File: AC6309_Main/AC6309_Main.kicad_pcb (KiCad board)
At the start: 2 copper layers, 8 parts, among them J1 Address Bus, J2 Data and Control, U1 HD63B09P, U2 W24257, U3 28C256, U4 74HCT00, U5 TMP68681, U6 MAX3232

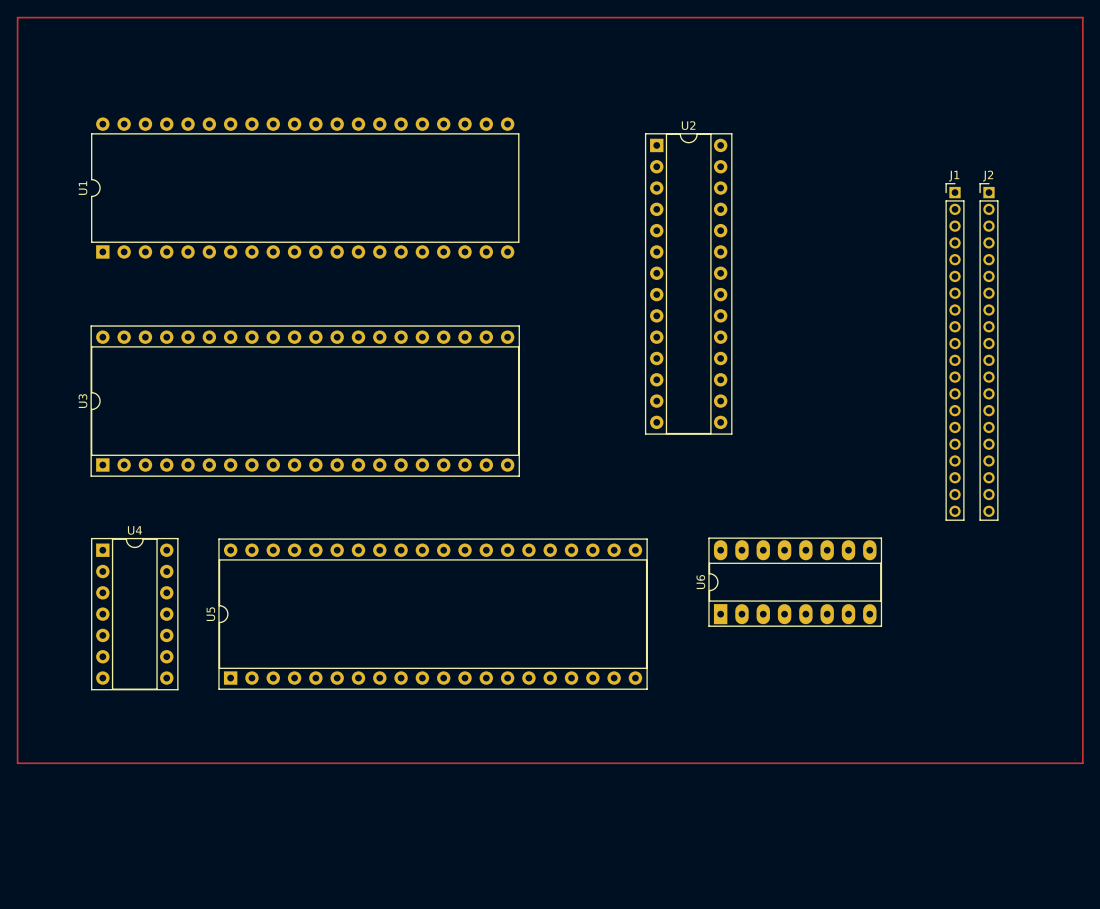
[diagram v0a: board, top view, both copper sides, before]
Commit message: Adding 74HC138 to the address decoder
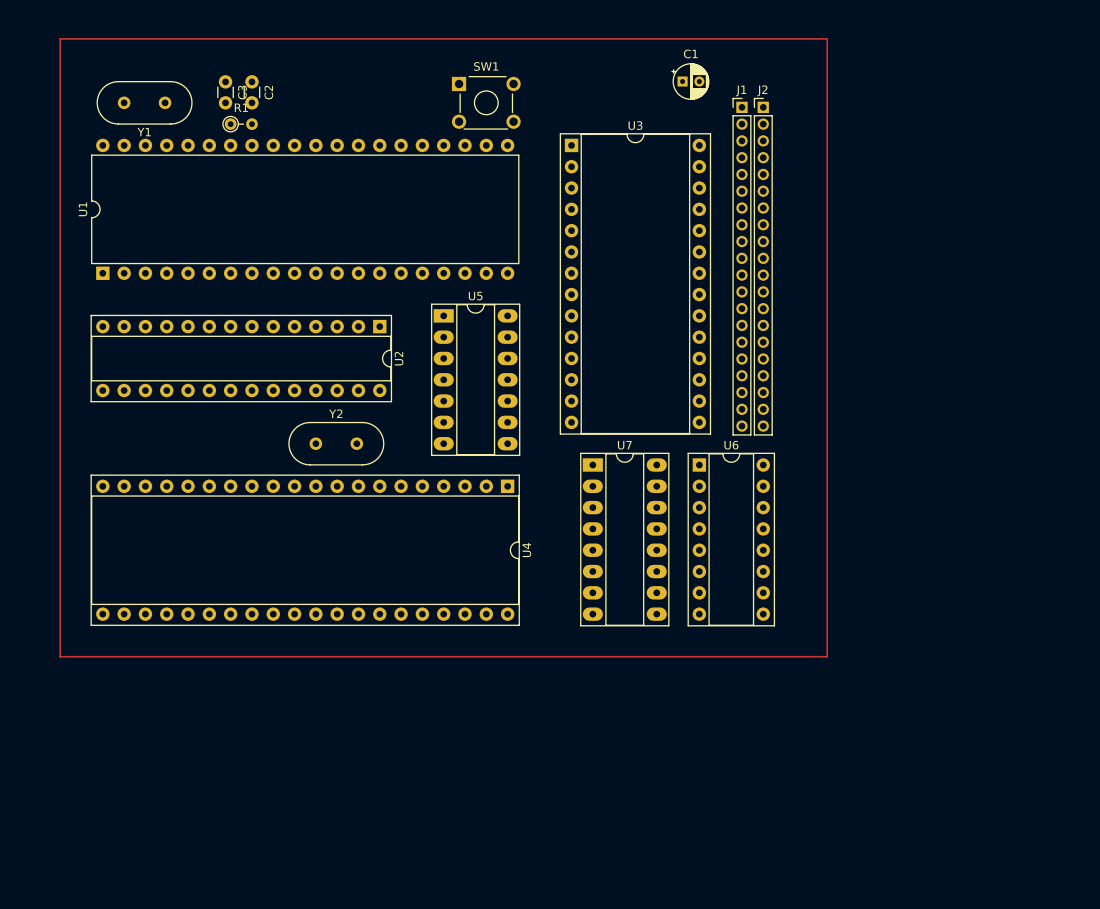
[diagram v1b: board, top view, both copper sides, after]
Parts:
- added C1: 100 uF, Capacitor_THT:CP_Radial_D4.0mm_P2.00mm, F.Cu at (119.9, 30.5)
- added C2: 15pF, Capacitor_THT:C_Disc_D3.0mm_W1.6mm_P2.50mm, F.Cu at (68.6, 30.5)
- added C3: 15pF, Capacitor_THT:C_Disc_D3.0mm_W1.6mm_P2.50mm, F.Cu at (65.4, 30.5)
- added R1: 2K2, Resistor_THT:R_Axial_DIN0204_L3.6mm_D1.6mm_P2.54mm_Vertical, F.Cu at (66.0, 35.6)
- added SW1: Reset, Button_Switch_THT:SW_TH_Tactile_Omron_B3F-10xx, F.Cu at (93.3, 30.8)
- added U6: 74HC138, Package_DIP:DIP-16_W7.62mm_Socket, F.Cu at (121.9, 76.2)
- added Y1: 7.3728 MHz, Crystal:Crystal_HC49-U_Vertical, F.Cu at (58.2, 33.0)
- added Y2: 1.8432 MHz, Crystal:Crystal_HC49-U_Vertical, F.Cu at (76.2, 73.7)
- J1: value Address Bus -> Address
- U3: footprint Package_DIP:DIP-40_W15.24mm_Socket -> Package_DIP:DIP-28_W15.24mm_Socket
- U5: renamed from U4; footprint Package_DIP:DIP-14_W7.62mm_Socket -> Package_DIP:DIP-14_W7.62mm_Socket_LongPads
- moved U3 67.6 mm to (106.7, 38.1), turned to 0 degrees
- moved U5 49.3 mm to (91.4, 58.4)
- moved U4 40.2 mm to (99.1, 78.7), turned to -90 degrees
- moved U2 39.5 mm to (83.8, 59.7), turned to -90 degrees
- moved J2 28.8 mm to (129.5, 33.6)
- moved J1 27.4 mm to (127.0, 33.6)
- moved U7 23.4 mm to (109.2, 76.2), turned to 0 degrees
- moved U1 2.54 mm to (50.8, 53.3)
- renumbered U5 to U4, U6 to U7
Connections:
- net Net-(U2-~{OE}) renamed //READ
- net Net-(U2-~{WE}) renamed //WRITE
- net Net-(U3-~{CS}) renamed //ROM_CS
- J2 pad 10: GND -> /8000_CS
- J2 pad 11: unconnected-(J2-Pin_11-Pad11) -> /9000_CS
- J2 pad 12: unconnected-(J2-Pin_12-Pad12) -> /A000_CS
- J2 pad 13: unconnected-(J2-Pin_13-Pad13) -> /B000_CS
- J2 pad 14: unconnected-(J2-Pin_14-Pad14) -> /R/W
- J2 pad 15: VCC -> unconnected-(J2-Pin_15-Pad15)
- U1 pad 32: Net-(U1-R/~{W}) -> /R/W
- U1 pad 34: Net-(U1-E) -> /E
- U1 pad 35: unconnected-(U1-Q-Pad35) -> /Q
- U1 pad 5: unconnected-(U1-BS-Pad5) -> /BS
- U1 pad 6: unconnected-(U1-BA-Pad6) -> /BA
- U4 pad 32: unconnected-(U5-X1/CLK-Pad32) -> Net-(U4-X1/CLK)
- U4 pad 33: unconnected-(U5-X2-Pad33) -> Net-(U4-X2)
- U5 pad 10: Net-(U1-E) -> Net-(U5-Pad10)
- U5 pad 11: Net-(U4-Pad11) -> Net-(U5-Pad10)
- U5 pad 12: Net-(U1-R/~{W}) -> /R/W
- U5 pad 13: Net-(U1-R/~{W}) -> /R/W
- U5 pad 4: Net-(U1-R/~{W}) -> /R/W
- U5 pad 5: Net-(U1-E) -> /E
- U5 pad 9: Net-(U4-Pad11) -> /E

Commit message: Added resistor networks. Updated PCB layout. Added temporary freeroute traces.
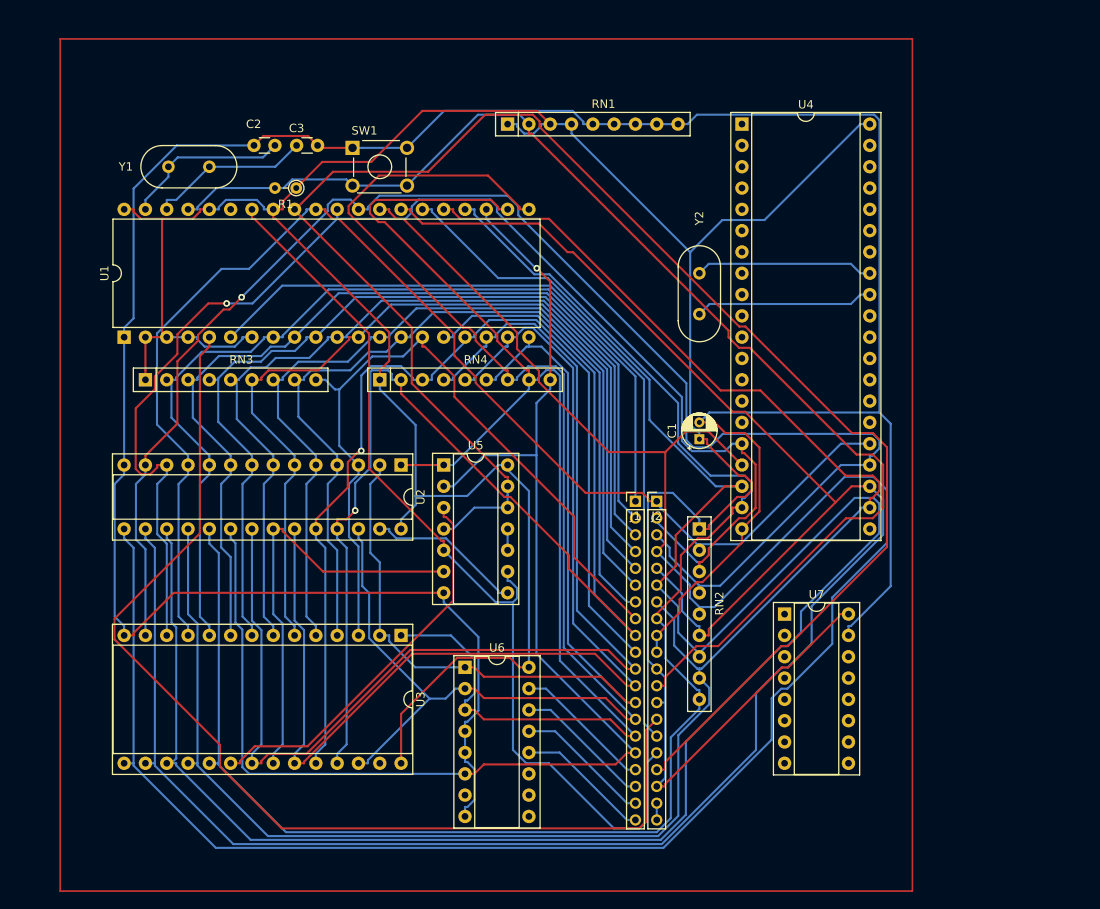
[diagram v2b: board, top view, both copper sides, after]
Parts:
- added RN1: R_Network08, Resistor_THT:R_Array_SIP9, F.Cu at (99.1, 35.6)
- added RN2: R_Network08, Resistor_THT:R_Array_SIP9, F.Cu at (121.9, 83.8)
- added RN3: R_Network08, Resistor_THT:R_Array_SIP9, F.Cu at (55.9, 66.0)
- added RN4: R_Network08, Resistor_THT:R_Array_SIP9, F.Cu at (83.8, 66.0)
- U5: footprint Package_DIP:DIP-14_W7.62mm_Socket_LongPads -> Package_DIP:DIP-14_W7.62mm_Socket
- U7: footprint Package_DIP:DIP-16_W7.62mm_Socket_LongPads -> Package_DIP:DIP-16_W7.62mm_Socket
- Y1, Y2: footprint Crystal:Crystal_HC49-U_Vertical -> Crystal:Crystal_HC49-4H_Vertical
- moved U3 61.9 mm to (86.4, 96.5), turned to -90 degrees
- moved U4 51.4 mm to (127.0, 35.6), turned to 0 degrees
- moved Y2 50.0 mm to (121.9, 53.3), turned to -90 degrees
- moved J1 48.6 mm to (114.3, 80.5)
- moved J2 48.6 mm to (116.8, 80.5)
- moved C1 42.7 mm to (121.9, 73.1), turned to 90 degrees
- moved U6 36.9 mm to (94.0, 100.3)
- moved U7 29.0 mm to (132.1, 94.0)
- moved U5 17.8 mm to (91.4, 76.2)
- moved U2 16.7 mm to (86.4, 76.2)
- moved SW1 14.8 mm to (80.6, 38.4)
- moved C3 11.4 mm to (73.9, 38.1), turned to 0 degrees
- moved R1 10.9 mm to (73.9, 43.2), turned to 180 degrees
- moved Y1 9.27 mm to (63.5, 40.6)
- moved C2 8.06 mm to (71.3, 38.1), turned to 180 degrees
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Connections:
- J1 pad 17: (no net) -> /8000_CS
- J1 pad 18: (no net) -> /9000_CS
- J1 pad 19: (no net) -> /A000_CS
- J1 pad 20: (no net) -> /B000_CS
- J2 pad 10: /8000_CS -> GND
- J2 pad 11: /9000_CS -> VCC
- J2 pad 12: /A000_CS -> //RESET
- J2 pad 13: /B000_CS -> VCC
- J2 pad 14: /R/W -> /BS
- J2 pad 15: unconnected-(J2-Pin_15-Pad15) -> /BA
- J2 pad 16: VCC -> /E
- J2 pad 17: (no net) -> /R/W
- J2 pad 18: (no net) -> VCC
- J2 pad 19: (no net) -> Net-(J2-Pin_19)
- J2 pad 20: (no net) -> Net-(J2-Pin_19)
- R1 pad 2: Net-(U1-~{RESET}) -> //RESET
- SW1 pad 2: Net-(U1-~{RESET}) -> //RESET
- U1 pad 37: Net-(U1-~{RESET}) -> //RESET
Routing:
- net VCC: track 0.00 -> 377.8 mm
- net GND: track 0.00 -> 345.5 mm
- net /D3: track 0.00 -> 262.4 mm
- net /D5: track 0.00 -> 254.8 mm
- net /D4: track 0.00 -> 253.6 mm
- net /D6: track 0.00 -> 219.1 mm
- net /R/W: track 0.00 -> 197.9 mm
- net /D7: track 0.00 -> 188.3 mm
- net /D2: track 0.00 -> 186.2 mm, vias 0 -> 1
- net /A13: track 0.00 -> 168.8 mm
- net /D1: track 0.00 -> 163.9 mm, vias 0 -> 1
- net /A15: track 0.00 -> 163.4 mm, vias 0 -> 1
- net /A14: track 0.00 -> 156.1 mm
- net /D0: track 0.00 -> 154.4 mm
- net /A8: track 0.00 -> 152.3 mm, vias 0 -> 1
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
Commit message: Replaced UART. Updates on Readme .
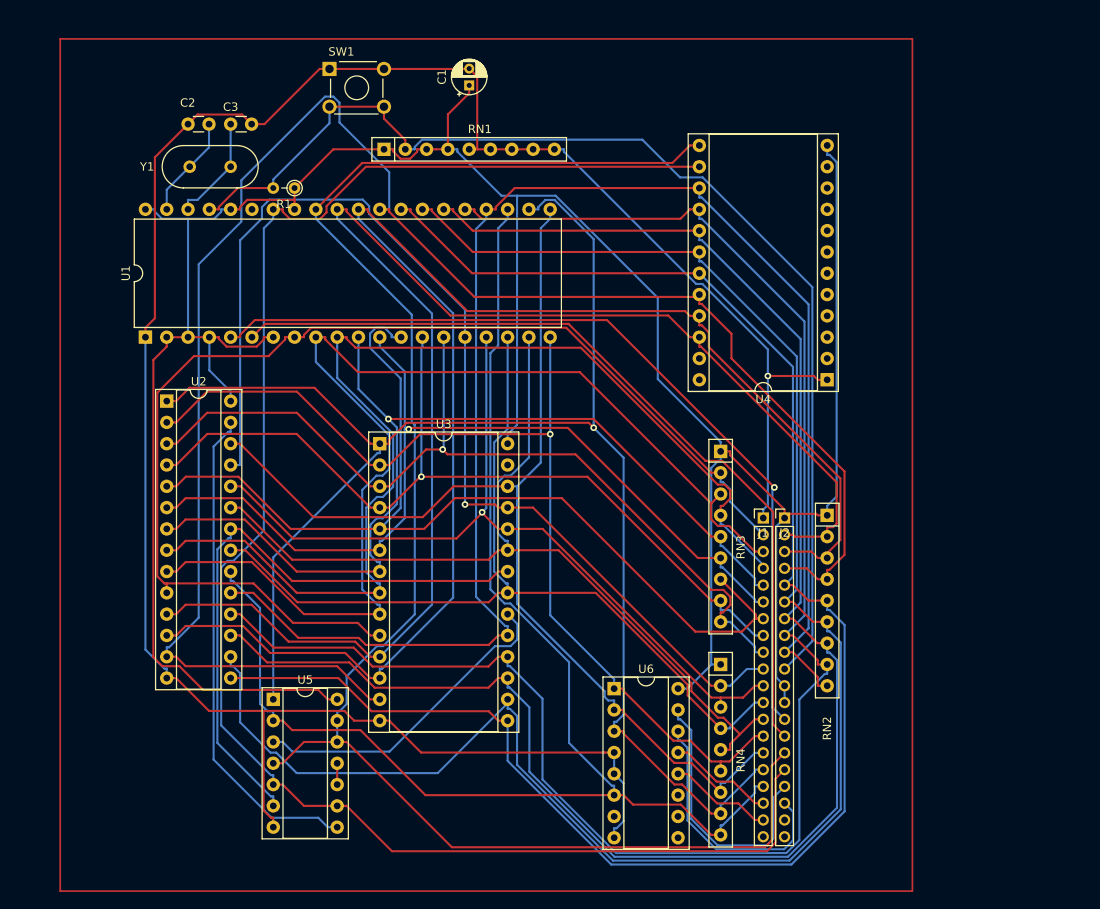
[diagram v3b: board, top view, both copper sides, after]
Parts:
- removed U7: MAX3232, Package_DIP:DIP-16_W7.62mm_Socket
- removed Y2: 1.8432 MHz, Crystal:Crystal_HC49-4H_Vertical
- U4: value TMP68681 -> MC68B50; footprint Package_DIP:DIP-40_W15.24mm_Socket -> Package_DIP:DIP-24_W15.24mm_Socket
- moved RN3 69.1 mm to (124.5, 74.6), turned to -90 degrees
- moved RN4 52.9 mm to (124.5, 100.0), turned to -90 degrees
- moved C1 50.3 mm to (94.5, 30.9)
- moved U5 34.5 mm to (71.1, 104.1)
- moved U4 32.1 mm to (137.2, 66.0), turned to 180 degrees
- moved U2 29.0 mm to (58.4, 68.6), turned to 0 degrees
- moved U3 23.0 mm to (83.8, 73.7), turned to 0 degrees
- moved U6 18.0 mm to (111.8, 102.9)
- moved J2 15.4 mm to (132.1, 82.5)
- moved J1 15.4 mm to (129.5, 82.5)
- moved RN2 15.3 mm to (137.2, 82.2)
- moved RN1 15.0 mm to (84.3, 38.6)
- moved SW1 9.80 mm to (77.8, 29.0)
- moved C3 8.26 mm to (66.0, 35.6)
- moved C2 8.26 mm to (63.5, 35.6)
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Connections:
- J1 pad 1: /A0 -> GND
- J1 pad 10: /A9 -> /A8
- J1 pad 11: /A10 -> /A9
- J1 pad 12: /A11 -> /A10
- J1 pad 13: /A12 -> /A11
- J1 pad 14: /A13 -> /A12
- J1 pad 15: /A14 -> /A13
- J1 pad 16: /A15 -> /A14
- J1 pad 17: /8000_CS -> /A15
- J1 pad 18: /9000_CS -> /A000_CS
- J1 pad 19: /A000_CS -> /B000_CS
- J1 pad 2: /A1 -> /A0
- J1 pad 20: /B000_CS -> unconnected-(J1-Pin_20-Pad20)
- J1 pad 3: /A2 -> /A1
- J1 pad 4: /A3 -> /A2
- J1 pad 5: /A4 -> /A3
- J1 pad 6: /A5 -> /A4
- J1 pad 7: /A6 -> /A5
- J1 pad 8: /A7 -> /A6
- J1 pad 9: /A8 -> /A7
- J2 pad 1: /D0 -> VCC
- J2 pad 10: GND -> //RESET
- J2 pad 12: //RESET -> VCC
- J2 pad 13: VCC -> /BS
- J2 pad 14: /BS -> /BA
- J2 pad 15: /BA -> /R/W
- J2 pad 17: /R/W -> /8000_CS
- J2 pad 18: VCC -> /9000_CS
- J2 pad 19: Net-(J2-Pin_19) -> unconnected-(J2-Pin_19-Pad19)
- J2 pad 2: /D1 -> /D0
- J2 pad 20: Net-(J2-Pin_19) -> unconnected-(J2-Pin_20-Pad20)
- J2 pad 3: /D2 -> /D1
- J2 pad 4: /D3 -> /D2
- J2 pad 5: /D4 -> /D3
- J2 pad 6: /D5 -> /D4
- J2 pad 7: /D6 -> /D5
- J2 pad 8: /D7 -> /D6
- J2 pad 9: GND -> /D7
- U4 pad 1: unconnected-(U4-A1-Pad1) -> GND
- U4 pad 12: unconnected-(U4-OP1-Pad12) -> VCC
- U4 pad 13: unconnected-(U4-OP3-Pad13) -> /R/W
- U4 pad 14: unconnected-(U4-OP5-Pad14) -> /E
- U4 pad 15: unconnected-(U4-OP7-Pad15) -> /D7
- U4 pad 16: /D1 -> /D6
- U4 pad 17: /D3 -> /D5
- U4 pad 18: /D5 -> /D4
- U4 pad 19: /D7 -> /D3
- U4 pad 20: GND -> /D2
- U4 pad 21: unconnected-(U4-INTRN-Pad21) -> /D1
- U4 pad 22: /D6 -> /D0
- U4 pad 23: /D4 -> unconnected-(U4-~{DCD}-Pad23)
- U4 pad 24: /D2 -> unconnected-(U4-~{CTS}-Pad24)
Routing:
- net /E: track 112.2 -> 201.5 mm
- net GND: track 345.5 -> 272.6 mm, vias 0 -> 1
- net /D3: track 262.4 -> 200.9 mm
- net /D5: track 254.8 -> 202.2 mm
- net /D4: track 253.6 -> 212.4 mm
- net //WRITE: track 18.7 -> 59.3 mm
- net /A13: track 168.8 -> 130.4 mm
- net /A10: track 142.0 -> 107.3 mm
- net /A14: track 156.1 -> 187.8 mm, vias 0 -> 1
- net /A11: track 136.0 -> 108.4 mm
- net /A0: track 113.2 -> 140.0 mm
- net /BS: track 128.0 -> 102.4 mm, vias 0 -> 1
- net /D2: track 186.2 -> 211.1 mm, vias 1 -> 0
- net VCC: track 377.8 -> 353.1 mm
- net /A1: track 111.7 -> 134.7 mm
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
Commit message: Schematics revision 1, Digital file, etc.
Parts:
- added J3: FTDI Header, Connector_PinHeader_2.54mm:PinHeader_1x06_P2.54mm_Vertical, F.Cu at (129.5, 116.8)
- J1, J2: footprint Connector_PinHeader_2.00mm:PinHeader_1x20_P2.00mm_Vertical -> Connector_PinHeader_2.54mm:PinHeader_1x20_P2.54mm_Vertical
- moved RN1 83.8 mm to (76.2, 121.9), turned to 180 degrees
- moved C1 83.0 mm to (121.9, 109.2)
- moved U5 70.8 mm to (53.3, 35.6)
- moved RN2 50.1 mm to (106.7, 121.9), turned to 180 degrees
- moved U4 44.2 mm to (102.9, 94.0), turned to 90 degrees
- moved J2 43.5 mm to (105.3, 116.8), turned to -90 degrees
- moved RN4 41.7 mm to (83.8, 109.2), turned to 180 degrees
- moved J1 39.9 mm to (105.3, 114.3), turned to -90 degrees
- moved RN3 36.1 mm to (114.3, 109.2), turned to 180 degrees
- moved C2 35.6 mm to (99.1, 35.7), turned to 90 degrees
- moved C3 33.1 mm to (99.1, 38.3), turned to -90 degrees
- moved SW1 30.7 mm to (107.8, 35.6)
- moved U2 30.6 mm to (61.0, 99.1), turned to 180 degrees
- moved U1 29.6 mm to (71.1, 35.6), turned to 0 degrees
- moved U6 26.2 mm to (87.6, 92.7), turned to -90 degrees
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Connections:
- J2 pad 11: VCC -> //NMI
- J2 pad 12: VCC -> //IRQ
- J2 pad 13: /BS -> //FIRQ
- J2 pad 14: /BA -> //HALT
- RN1 pad 3: VCC -> //NMI
- RN1 pad 4: VCC -> //IRQ
- RN1 pad 5: GND -> //FIRQ
- RN1 pad 6: GND -> //DMABREQ
- RN1 pad 7: GND -> //HALT
- RN1 pad 8: GND -> /MRDY
- U1 pad 2: VCC -> //NMI
- U1 pad 3: VCC -> //IRQ
- U1 pad 33: VCC -> //DMABREQ
- U1 pad 36: VCC -> /MRDY
- U1 pad 4: VCC -> //FIRQ
- U1 pad 40: VCC -> //HALT
- U1 pad 5: /BS -> unconnected-(U1-BS-Pad5)
- U1 pad 6: /BA -> unconnected-(U1-BA-Pad6)
- U4 pad 10: unconnected-(U4-CS1-Pad10) -> /A13
- U4 pad 11: unconnected-(U4-RS-Pad11) -> /A0
- U4 pad 2: unconnected-(U4-Rx_Data-Pad2) -> Net-(J3-Pin_3)
- U4 pad 23: unconnected-(U4-~{DCD}-Pad23) -> GND
- U4 pad 24: unconnected-(U4-~{CTS}-Pad24) -> Net-(U4-~{CTS})
- U4 pad 3: unconnected-(U4-Rx_CLK-Pad3) -> /E
- U4 pad 4: unconnected-(U4-Tx_CLK-Pad4) -> /E
- U4 pad 5: unconnected-(U4-~{RTS}-Pad5) -> Net-(U4-~{CTS})
- U4 pad 6: unconnected-(U4-Tx_Data-Pad6) -> Net-(J3-Pin_2)
- U4 pad 7: unconnected-(U4-~{IRQ}-Pad7) -> //IRQ
- U4 pad 8: unconnected-(U4-CS0-Pad8) -> /A15
- U4 pad 9: unconnected-(U4-CS2-Pad9) -> /A14
- U6 pad 11: unconnected-(U6-~{Y4}-Pad11) -> /C000_CS
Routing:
- net //HALT: track 0.00 -> 147.5 mm
- net //IRQ: track 0.00 -> 147.0 mm, vias 0 -> 2
- net //NMI: track 0.00 -> 137.9 mm, vias 0 -> 1
- net //FIRQ: track 0.00 -> 124.6 mm, vias 0 -> 1
- net /BS: track 102.4 -> 0.00 mm, vias 1 -> 0
- net /D4: track 212.4 -> 312.4 mm, vias 0 -> 1
- net /BA: track 99.4 -> 0.00 mm
- net /A11: track 108.4 -> 207.1 mm, vias 0 -> 1
- net //DMABREQ: track 0.00 -> 94.5 mm, vias 0 -> 1
- net /MRDY: track 0.00 -> 87.9 mm
- net VCC: track 353.1 -> 275.6 mm, vias 0 -> 2
- net /A13: track 130.4 -> 200.5 mm, vias 0 -> 3
- net /A6: track 103.0 -> 163.4 mm, vias 1 -> 3
- net /D7: track 185.1 -> 245.4 mm, vias 0 -> 1
- net /A2: track 131.0 -> 187.0 mm, vias 0 -> 1
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- added copper zone on B.Cu, net GND
- added copper zone on F.Cu, net GND
